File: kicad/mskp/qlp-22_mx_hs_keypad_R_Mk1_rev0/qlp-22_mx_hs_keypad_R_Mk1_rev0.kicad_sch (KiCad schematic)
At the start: 23 parts, among them J1 Conn_01x12_Socket, SW1 Switch, SW10 Switch, SW11 Switch, SW2 Switch, SW3 Switch, SW4 Switch, SW5 Switch, SW6 Switch, SW7 Switch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

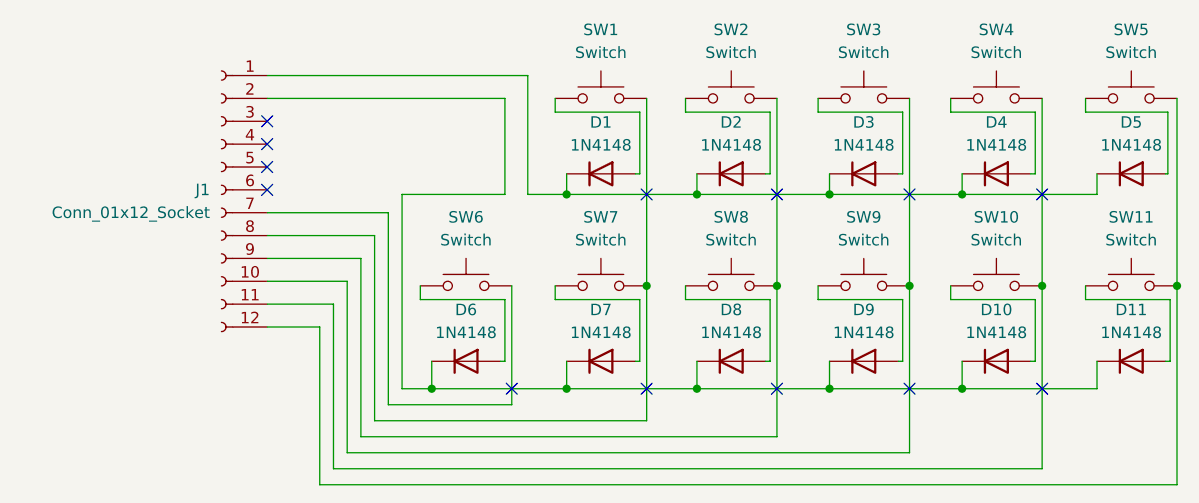
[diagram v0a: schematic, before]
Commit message: Adds wiring for qlp-22_mx_hs_keypad_R_Mk1_rev0
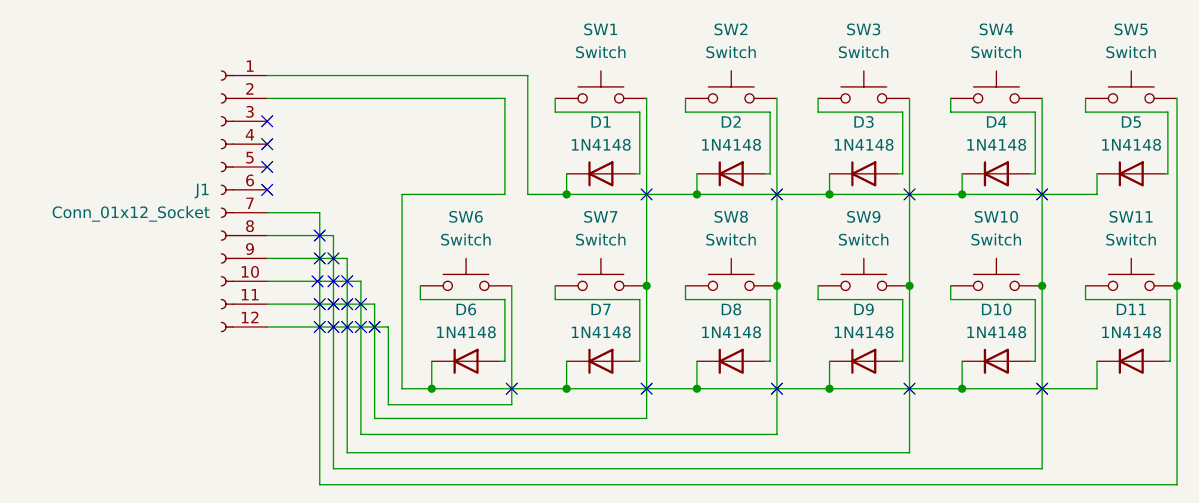
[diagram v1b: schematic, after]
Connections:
- net at SW2.2, SW8.2: now also J1.10 (Pin_10); no longer J1.9 (Pin_9)
- net at SW11.2, SW5.2: now also J1.7 (Pin_7); no longer J1.12 (Pin_12)
- net at SW1.2, SW7.2: now also J1.11 (Pin_11); no longer J1.8 (Pin_8)
- net at SW10.2, SW4.2: now also J1.8 (Pin_8); no longer J1.11 (Pin_11)
- net at SW3.2, SW9.2: now also J1.9 (Pin_9); no longer J1.10 (Pin_10)
- net at SW6.2: now also J1.12 (Pin_12); no longer J1.7 (Pin_7)
- no-connect marks 13 -> 28
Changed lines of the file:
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@@
   (junction (at 131.318 122.682) (diameter 0) (color 0 0 0 0)
   )
+  (no_connect (at 121.92 113.284))
+  (no_connect (at 121.92 110.744))
+  (no_connect (at 120.396 115.824))
+  (no_connect (at 118.872 115.824))
   (no_connect (at 184.404 122.682))
   (no_connect (at 140.208 122.682))
+  (no_connect (at 118.872 113.284))
   (no_connect (at 113.03 100.584))
+  (no_connect (at 118.618 110.744))
+  (no_connect (at 120.396 108.204))
+  (no_connect (at 121.92 115.824))
   (no_connect (at 113.03 95.504))
   (no_connect (at 184.404 101.092))
+  (no_connect (at 120.396 113.284))
   (no_connect (at 169.672 101.092))
   (no_connect (at 169.672 122.682))
+  (no_connect (at 118.872 108.204))
+  (no_connect (at 118.872 105.664))
   (no_connect (at 199.136 101.092))
   (no_connect (at 199.136 122.682))
   (no_connect (at 113.03 98.044))
+  (no_connect (at 124.968 115.824))
+  (no_connect (at 123.444 115.824))
   (no_connect (at 155.194 101.092))
+  (no_connect (at 120.396 110.744))
   (no_connect (at 113.03 92.964))
   (no_connect (at 155.194 122.682))
+  (no_connect (at 123.444 113.284))
   (wire (pts (xy 159.512 111.252) (xy 159.512 112.776))
     (stroke (width 0) (type default))
   )
-  (wire (pts (xy 118.872 115.824) (xy 113.03 115.824))
-    (stroke (width 0) (type default))
-  )
   (wire (pts (xy 184.404 111.252) (xy 184.404 129.794))
     (stroke (width 0) (type default))
   )
-  (wire (pts (xy 113.03 110.744) (xy 121.92 110.744))
+  (wire (pts (xy 113.03 110.744) (xy 123.444 110.744))
     (stroke (width 0) (type default))
   )
@@
     (stroke (width 0) (type default))
   )
-  (wire (pts (xy 140.208 111.252) (xy 140.208 124.46))
-    (stroke (width 0) (type default))
-  )
   (wire (pts (xy 214.122 133.35) (xy 118.872 133.35))
     (stroke (width 0) (type default))
@@
     (stroke (width 0) (type default))
   )
-  (wire (pts (xy 126.492 124.46) (xy 126.492 103.124))
-    (stroke (width 0) (type default))
-  )
   (wire (pts (xy 197.866 119.634) (xy 198.374 119.634))
     (stroke (width 0) (type default))
@@
     (stroke (width 0) (type default))
   )
-  (wire (pts (xy 118.872 133.35) (xy 118.872 115.824))
+  (wire (pts (xy 118.872 103.124) (xy 118.872 133.35))
     (stroke (width 0) (type default))
   )
@@
     (stroke (width 0) (type default))
   )
+  (wire (pts (xy 126.492 115.824) (xy 126.492 124.46))
+    (stroke (width 0) (type default))
+  )
   (wire (pts (xy 160.782 101.092) (xy 146.304 101.092))
     (stroke (width 0) (type default))
   )
-  (wire (pts (xy 124.968 126.238) (xy 124.968 105.664))
-    (stroke (width 0) (type default))
-  )
-  (wire (pts (xy 169.672 128.016) (xy 123.444 128.016))
+  (wire (pts (xy 169.672 127.762) (xy 123.444 127.762))
     (stroke (width 0) (type default))
   )
@@
     (stroke (width 0) (type default))
   )
-  (wire (pts (xy 140.208 124.46) (xy 126.492 124.46))
+  (wire (pts (xy 118.872 103.124) (xy 113.03 103.124))
     (stroke (width 0) (type default))
   )
@@
     (stroke (width 0) (type default))
   )
-  (wire (pts (xy 123.444 108.204) (xy 113.03 108.204))
-    (stroke (width 0) (type default))
-  )
   (wire (pts (xy 183.642 91.948) (xy 183.642 98.806))
     (stroke (width 0) (type default))
   )
-  (wire (pts (xy 113.03 105.664) (xy 124.968 105.664))
-    (stroke (width 0) (type default))
-  )
   (wire (pts (xy 175.514 122.682) (xy 160.782 122.682))
     (stroke (width 0) (type default))
   )
+  (wire (pts (xy 113.03 113.284) (xy 124.968 113.284))
+    (stroke (width 0) (type default))
+  )
+  (wire (pts (xy 140.208 124.46) (xy 140.208 111.252))
+    (stroke (width 0) (type default))
+  )
+  (wire (pts (xy 124.968 125.984) (xy 124.968 113.284))
+    (stroke (width 0) (type default))
+  )
   (wire (pts (xy 155.194 90.424) (xy 155.194 111.252))
     (stroke (width 0) (type default))
@@
     (stroke (width 0) (type default))
   )
-  (wire (pts (xy 126.492 103.124) (xy 113.03 103.124))
-    (stroke (width 0) (type default))
-  )
   (wire (pts (xy 154.432 119.634) (xy 153.924 119.634))
     (stroke (width 0) (type default))
   )
+  (wire (pts (xy 121.92 108.204) (xy 113.03 108.204))
+    (stroke (width 0) (type default))
+  )
   (wire (pts (xy 190.246 98.806) (xy 190.246 101.092))
     (stroke (width 0) (type default))
@@
     (stroke (width 0) (type default))
   )
-  (wire (pts (xy 121.92 129.794) (xy 121.92 110.744))
+  (wire (pts (xy 121.92 108.204) (xy 121.92 129.794))
     (stroke (width 0) (type default))
   )
@@
     (stroke (width 0) (type default))
   )
+  (wire (pts (xy 120.396 105.664) (xy 113.03 105.664))
+    (stroke (width 0) (type default))
+  )
+  (wire (pts (xy 123.444 127.762) (xy 123.444 110.744))
+    (stroke (width 0) (type default))
+  )
   (wire (pts (xy 168.91 119.634) (xy 168.402 119.634))
     (stroke (width 0) (type default))
@@
     (stroke (width 0) (type default))
   )
+  (wire (pts (xy 113.03 115.824) (xy 126.492 115.824))
+    (stroke (width 0) (type default))
+  )
   (wire (pts (xy 146.304 119.634) (xy 146.304 122.682))
     (stroke (width 0) (type default))
@@
     (stroke (width 0) (type default))
   )
-  (wire (pts (xy 169.672 111.252) (xy 169.672 128.016))
-    (stroke (width 0) (type default))
-  )
-  (wire (pts (xy 155.194 126.238) (xy 124.968 126.238))
+  (wire (pts (xy 169.672 111.252) (xy 169.672 127.762))
+    (stroke (width 0) (type default))
+  )
+  (wire (pts (xy 155.194 125.984) (xy 124.968 125.984))
     (stroke (width 0) (type default))
   )
@@
     (stroke (width 0) (type default))
   )
-  (wire (pts (xy 155.194 111.252) (xy 155.194 126.238))
+  (wire (pts (xy 155.194 111.252) (xy 155.194 125.984))
     (stroke (width 0) (type default))
   )
@@
     (stroke (width 0) (type default))
   )
-  (wire (pts (xy 123.444 128.016) (xy 123.444 108.204))
-    (stroke (width 0) (type default))
-  )
   (wire (pts (xy 183.642 112.776) (xy 183.642 119.634))
     (stroke (width 0) (type default))
@@
     (stroke (width 0) (type default))
   )
+  (wire (pts (xy 126.492 124.46) (xy 140.208 124.46))
+    (stroke (width 0) (type default))
+  )
   (wire (pts (xy 213.36 112.776) (xy 213.36 119.634))
     (stroke (width 0) (type default))
@@
     (stroke (width 0) (type default))
   )
-  (wire (pts (xy 120.396 131.572) (xy 120.396 113.284))
+  (wire (pts (xy 120.396 105.664) (xy 120.396 131.572))
     (stroke (width 0) (type default))
   )
@@
     (stroke (width 0) (type default))
   )
-  (wire (pts (xy 120.396 113.284) (xy 113.03 113.284))
-    (stroke (width 0) (type default))
-  )
